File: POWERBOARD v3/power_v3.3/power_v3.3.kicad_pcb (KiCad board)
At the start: 4 copper layers, 60 x 34.1 mm, 63 parts, among them IC1 MAX25301AATB_V+T, IC2 MCP6541T-I_OT, IC3 AP2281-1FMG-7, J1 43650-0300, J2 UJ20-C-H-G-SMT-1-P16-TR, J3 2053380002, U1 USBLC6-2, U2 BQ25886RGE, U3 TPS62160DSG

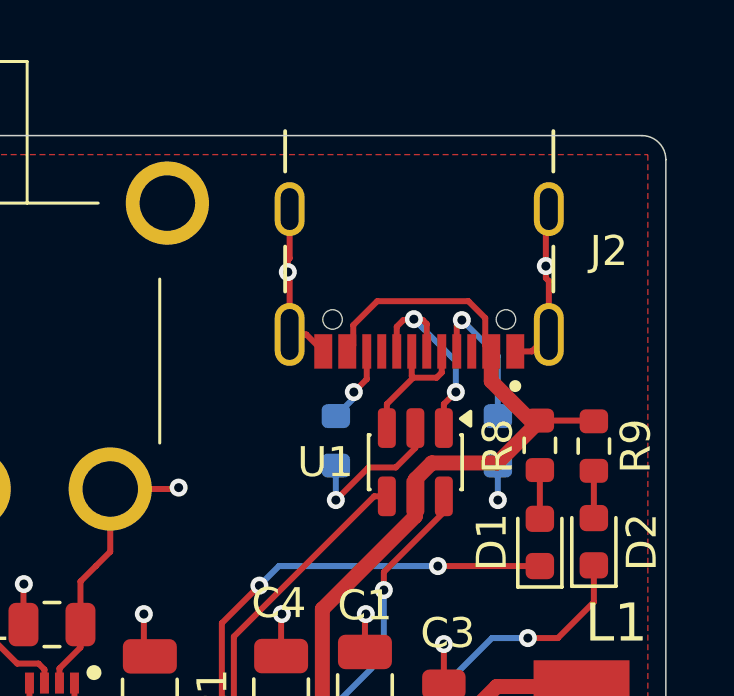
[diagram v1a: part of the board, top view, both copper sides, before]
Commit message: Routed new USB-C connector
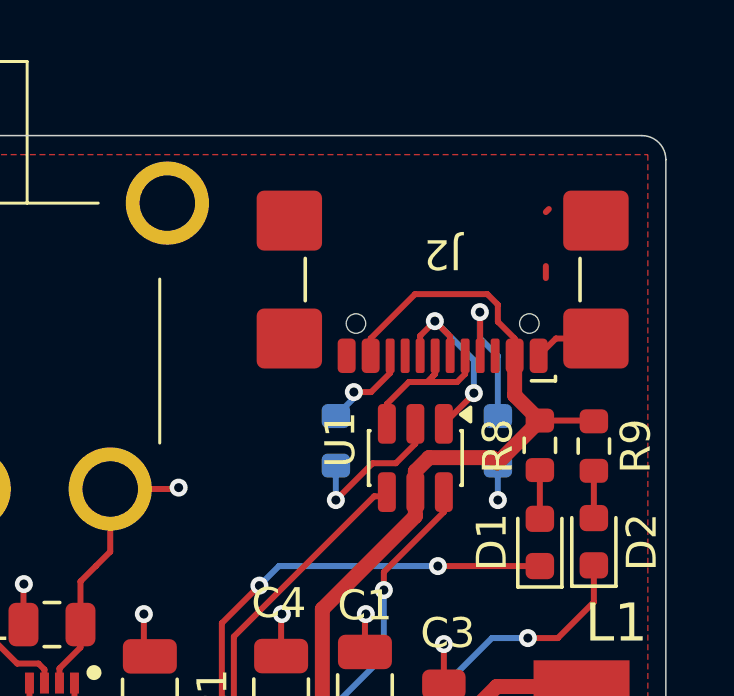
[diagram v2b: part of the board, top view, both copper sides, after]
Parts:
- J2: value UJ20-C-H-G-SMT-1-P16-TR -> USB_C_Receptacle_USB2.0_16P; footprint UJ20_C_H_G_SMT_1_P16_TR:SAMESKY_UJ20-C-H-G-SMT-1-P16-TR -> Connector_USB:USB_C_Receptacle_GCT_USB4110
- moved J2 3.89 mm to (184.0, 72.6)
- moved U1 0.14 mm to (183.1, 79.7)
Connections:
- net Net-(J2-DN1) renamed /Charging circuit/USB_D-
- net Net-(J2-DP1) renamed /Charging circuit/USB_D+
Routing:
- net GND: track 67.9 -> 60.0 mm, vias 38 -> 36
- net /Charging circuit/USB_D-: track 4.67 -> 5.28 mm
- net /Charging circuit/CC2: track 2.58 -> 3.10 mm

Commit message: Added GND vias around USB-C connector
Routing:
- net GND: track 60.0 -> 77.7 mm, vias 36 -> 38
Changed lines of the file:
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@@
+	)
+	(segment
+		(start 187.16 76.305)
+		(end 188.605 77.75)
+		(width 0.2)
+		(layer "F.Cu")
+		(net "GND")
 	)
 	(segment
@@
 	)
 	(segment
+		(start 179.45 77.7)
+		(end 179.45 77.615)
+		(width 0.2)
+		(layer "F.Cu")
+		(net "GND")
+	)
+	(segment
 		(start 185.05 95.765)
 		(end 184.075 94.79)
@@
 	)
 	(segment
-		(start 187.4 71.515)
-		(end 187.5 71.415)
-		(width 0.2)
-		(layer "F.Cu")
-		(net "GND")
-	)
-	(segment
 		(start 161.9 85.815)
 		(end 161.4 85.315)
@@
 	)
 	(segment
-		(start 187.4 73.315)
-		(end 187.4 73.715)
-		(width 0.2)
-		(layer "F.Cu")
-		(net "GND")
-	)
-	(segment
 		(start 189.9 94.885)
 		(end 189.83 94.815)
@@
 	)
 	(segment
+		(start 189.07 76.52)
+		(end 190.3 77.75)
+		(width 0.2)
+		(layer "F.Cu")
+		(net "GND")
+	)
+	(segment
 		(start 178.575 84.94)
 		(end 178.6 84.915)
@@
 	)
 	(segment
+		(start 178.85 75.73)
+		(end 178.85 77.1)
+		(width 0.2)
+		(layer "F.Cu")
+		(net "GND")
+	)
+	(segment
+		(start 178.85 77.1)
+		(end 179.45 77.7)
+		(width 0.2)
+		(layer "F.Cu")
+		(net "GND")
+	)
+	(segment
 		(start 187.16 76.305)
 		(end 187.735 75.73)
@@
 	)
 	(segment
+		(start 178.85 75.73)
+		(end 178.85 71.8)
+		(width 0.2)
+		(layer "F.Cu")
+		(net "GND")
+	)
+	(segment
 		(start 178.575 86.315)
 		(end 178.575 84.94)
@@
 	)
 	(segment
+		(start 179.45 77.615)
+		(end 180.76 76.305)
+		(width 0.2)
+		(layer "F.Cu")
+		(net "GND")
+	)
+	(segment
+		(start 189.07 71.8)
+		(end 189.07 75.73)
+		(width 0.2)
+		(layer "F.Cu")
+		(net "GND")
+	)
+	(segment
+		(start 189.07 75.73)
+		(end 189.07 76.52)
+		(width 0.2)
+		(layer "F.Cu")
+		(net "GND")
+	)
+	(segment
 		(start 177.8625 93.1275)
 		(end 177.8625 92.6275)
@@
 	)
 	(segment
+		(start 188.605 77.75)
+		(end 190.3 77.75)
+		(width 0.2)
+		(layer "F.Cu")
+		(net "GND")
+	)
+	(segment
 		(start 185.05 95.89)
 		(end 185.05 95.765)
@@
 	)
 	(via
+		(at 179.45 77.7)
+		(size 0.6)
+		(drill 0.3)
+		(layers "F.Cu" "B.Cu")
+		(free yes)
+		(net "GND")
+	)
+	(via
 		(at 180.465 93.6)
 		(size 0.6)
@@
 		(size 0.6)
 		(drill 0.3)
+		(layers "F.Cu" "B.Cu")
+		(free yes)
+		(net "GND")
+	)
+	(via
+		(at 190.3 77.75)
+		(size 0.6)
+		(drill 0.3)

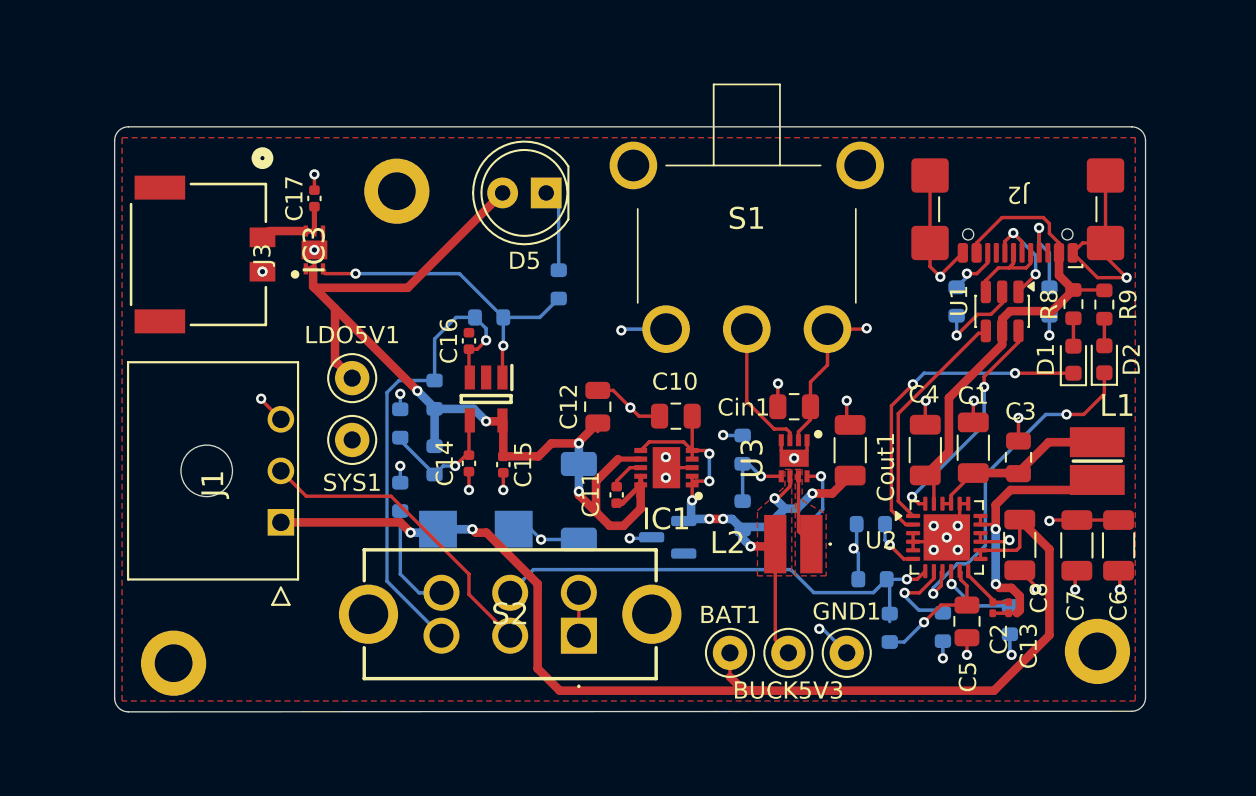
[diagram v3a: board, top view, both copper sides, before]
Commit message: [fix]: reviewed powerboard, modified zone priority
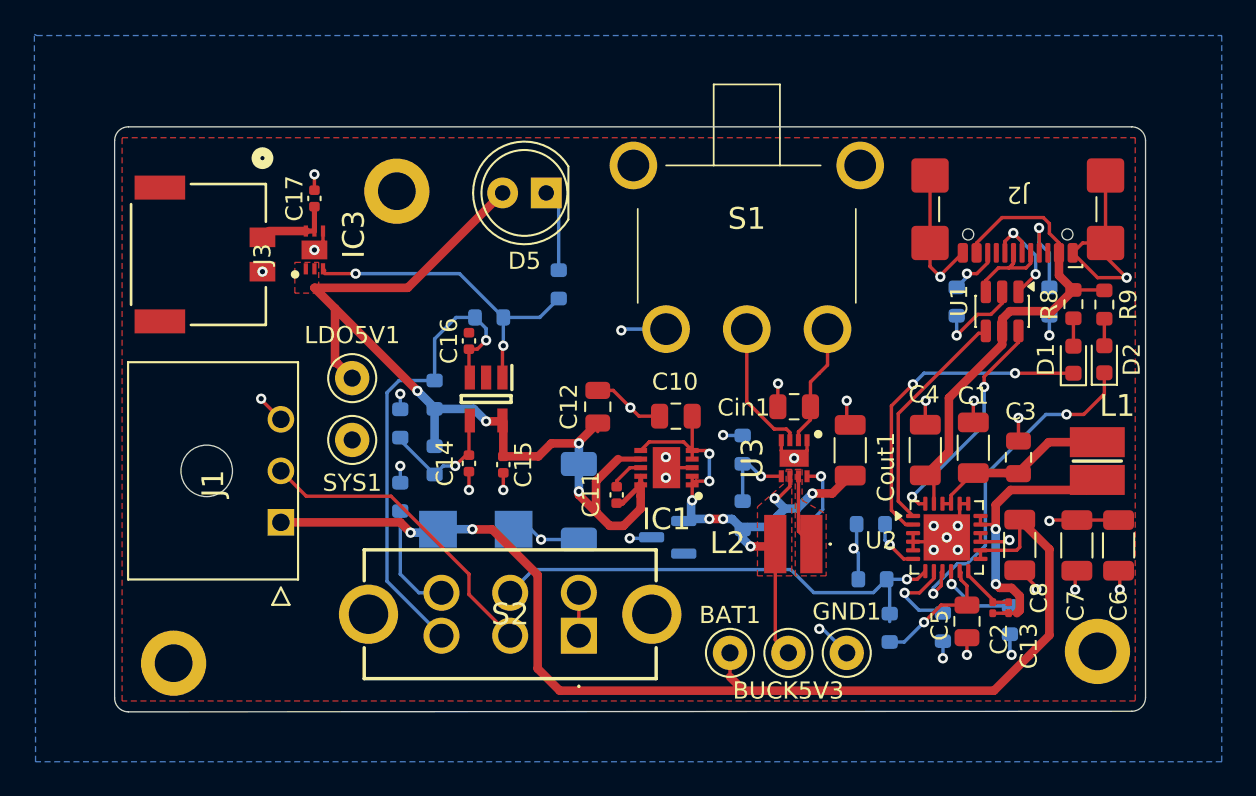
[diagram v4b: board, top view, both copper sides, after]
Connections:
- net Net-(IC3-OUT_1) renamed /5.3 to 5V/5V_out
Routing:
- net /Charging circuit/SYS: track 15.9 -> 13.6 mm, vias 3 -> 2
- net /5.3 to 5V/output_at_5: track 61.3 -> 59.6 mm
- net /Charging circuit/BATTERY VOLTAGE: track 69.7 -> 68.0 mm
- added copper zone on F.Cu, net /5.3 to 5V/output_at_5
- added copper zone on B.Cu, net GND
